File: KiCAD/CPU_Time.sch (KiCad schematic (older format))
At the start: 11 parts, among them P1 JST_connector, SW1 Reset, U1 NUCLEO64-F411RE, U2 DS3231, U3 MAS6180

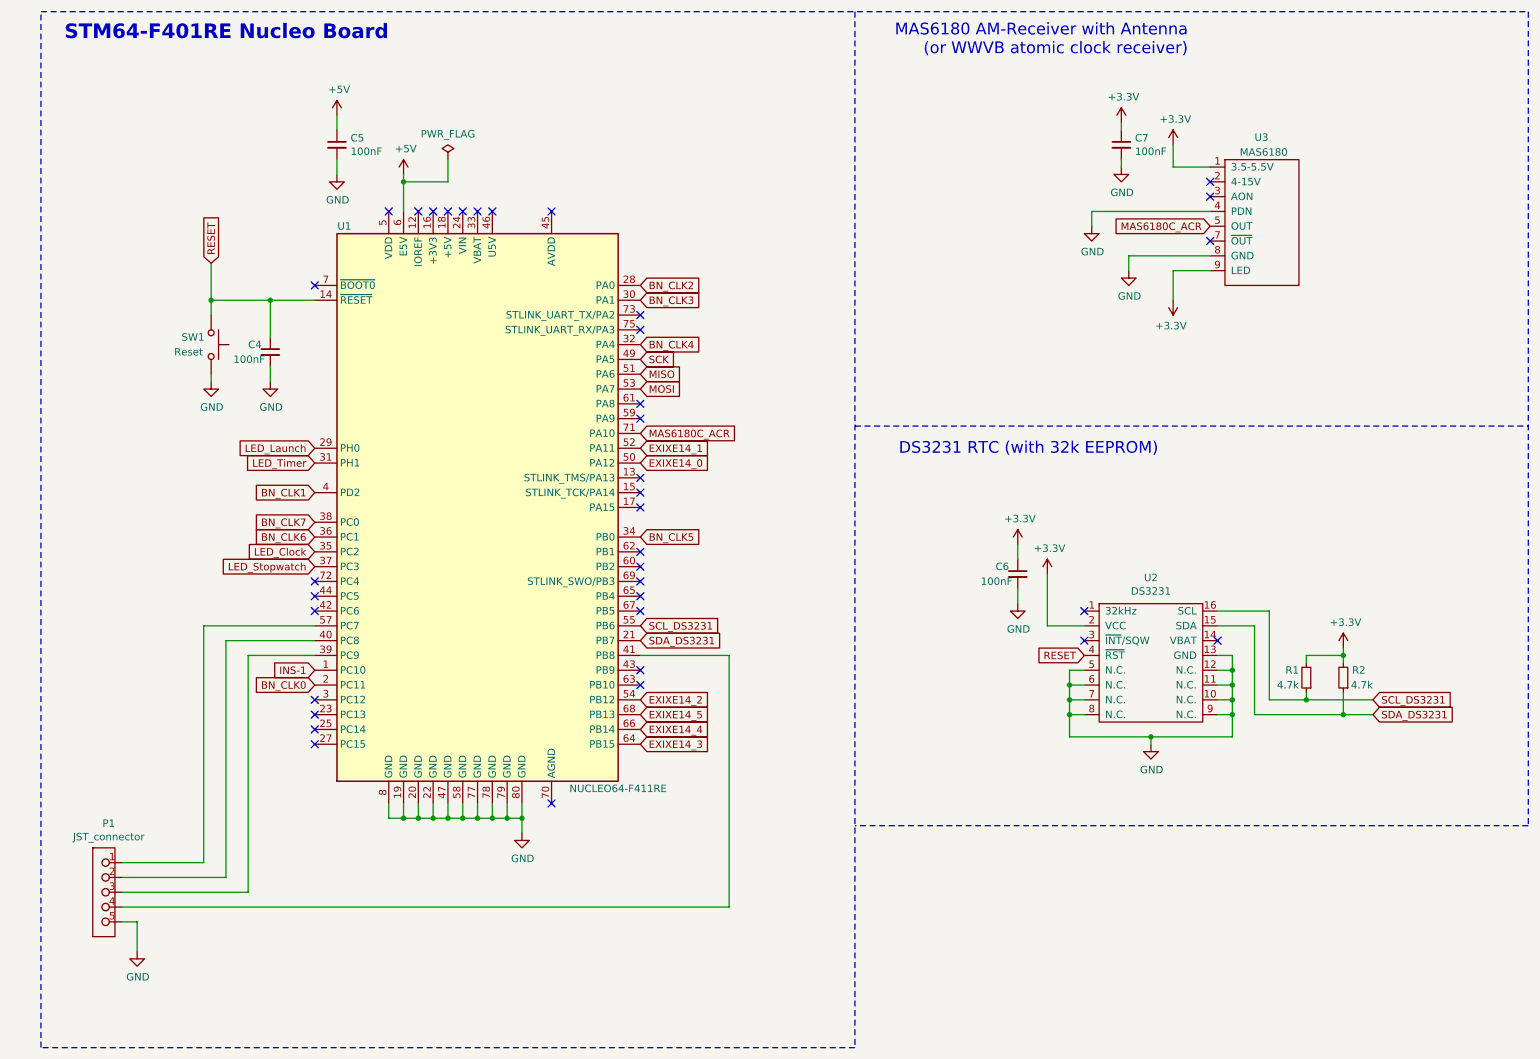
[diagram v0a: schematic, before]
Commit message: v01.2: Updated component numbers, title block, and added transistor library.
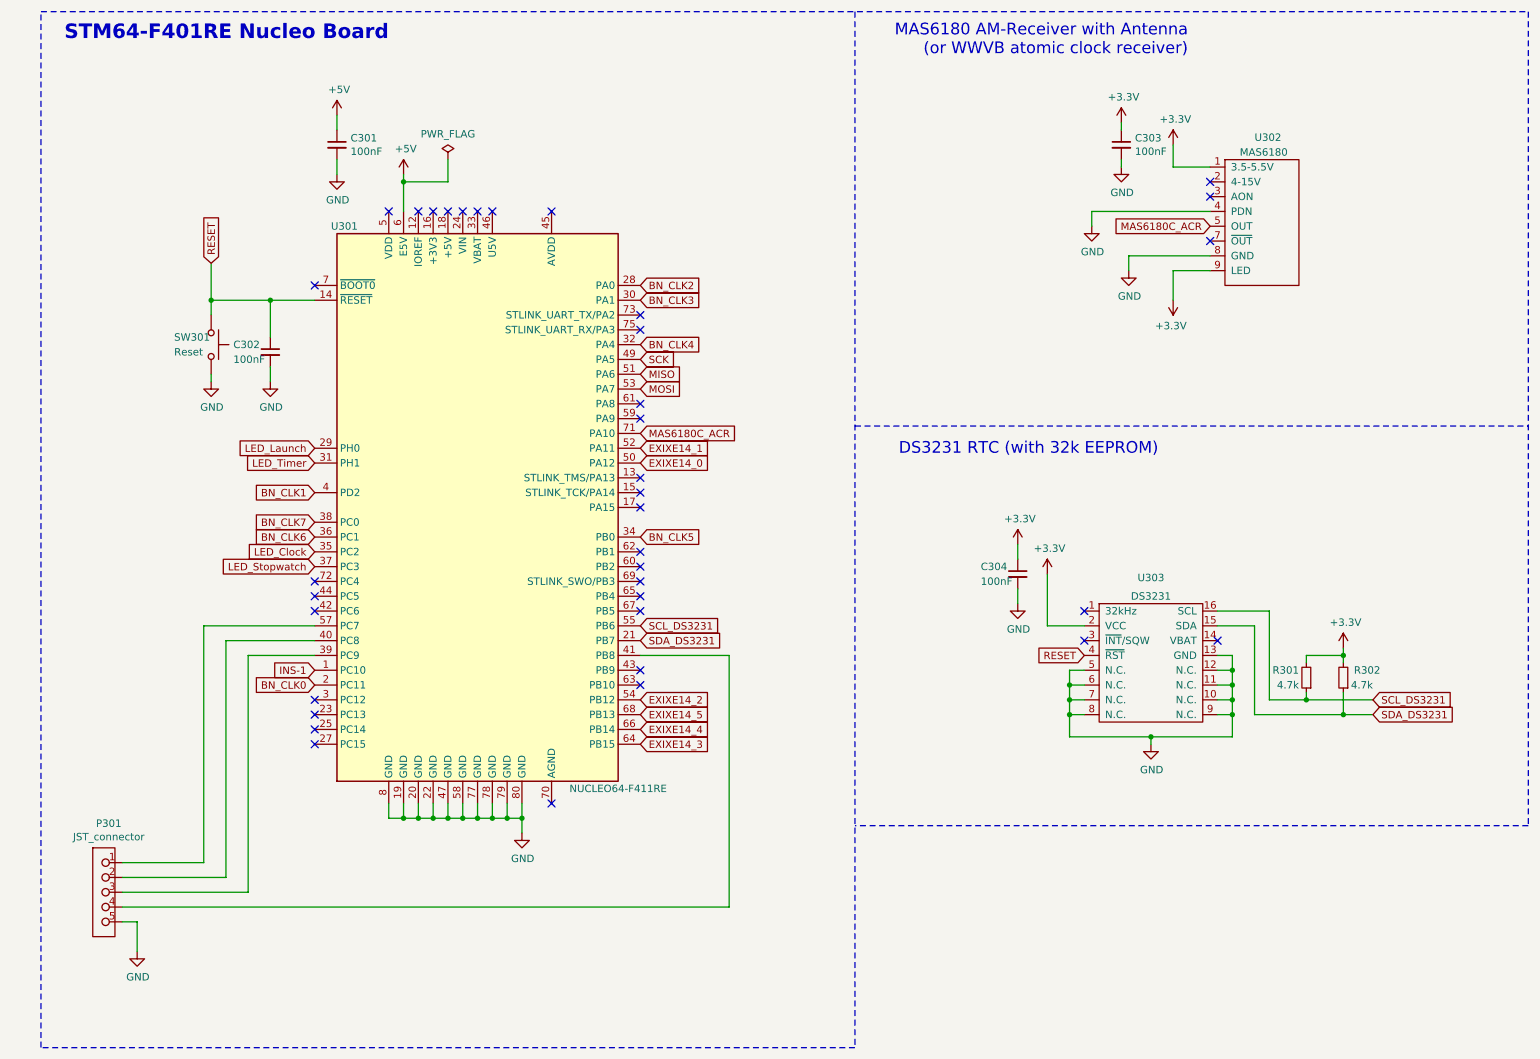
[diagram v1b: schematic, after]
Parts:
- renumbered C5 to C301, C4 to C302, C7 to C303, C6 to C304, P1 to P301, R1 to R301, R2 to R302, SW1 to SW301, U1 to U301, U3 to U302, U2 to U303
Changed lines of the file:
@@
 Sheet 3 5
 Title "Nixie Tube Clock Host Board"
-Date "2021-04-20"
-Rev "v01.1"
+Date "2021-04-26"
+Rev "v01.2"
 Comp "University of Alberta (AlbertaSat)"
-Comment1 "License: CC BY 4.0 (https://creativecommons.org/licenses/by/4.0/)"
-Comment2 "Steven Knudsen (ECE dept., Faculty of Engineering, University of Alberta)."
-Comment3 "This schematic was designed with the assistance of "
-Comment4 "Author: Pundeep Hundal                   Co-author: Sichun Xu"
+Comment1 ""
+Comment2 "License: CC BY 4.0 (https://creativecommons.org/licenses/by/4.0/)"
+Comment3 "Co-author: Sichun Xu"
+Comment4 "Author: Pundeep Hundal"
 $EndDescr
 $Comp
@@
 P 2550 2800
 AR Path="/6096D84C" Ref="C?"  Part="1"
-AR Path="/6091BF76/6096D84C" Ref="C4"  Part="1"
-F 0 "C4" H 2400 2850 50  0000 L CNN
+AR Path="/6091BF76/6096D84C" Ref="C302"  Part="1"
+F 0 "C302" H 2300 2850 50  0000 L CNN
 F 1 "100nF" H 2300 2750 50  0000 L CNN
 F 2 "" H 2550 2800 50  0001 C CNN
@@
 P 2150 2750
 AR Path="/6096D859" Ref="SW?"  Part="1"
-AR Path="/6091BF76/6096D859" Ref="SW1"  Part="1"
-F 0 "SW1" V 2100 2550 50  0000 L CNN
+AR Path="/6091BF76/6096D859" Ref="SW301"  Part="1"
+F 0 "SW301" V 2100 2500 50  0000 L CNN
 F 1 "Reset" V 2200 2500 50  0000 L CNN
 F 2 "" H 2150 2950 50  0001 C CNN
@@
 P 9250 1800
 AR Path="/6096D892" Ref="U?"  Part="1"
-AR Path="/6091BF76/6096D892" Ref="U3"  Part="1"
-F 0 "U3" H 9200 2250 50  0000 L CNN
+AR Path="/6091BF76/6096D892" Ref="U302"  Part="1"
+F 0 "U302" H 9200 2250 50  0000 L CNN
 F 1 "MAS6180" H 9100 2150 50  0000 L CNN
 F 2 "" H 9250 1800 50  0001 C CNN
@@
 P 7600 4300
 AR Path="/6096D898" Ref="C?"  Part="1"
-AR Path="/6091BF76/6096D898" Ref="C6"  Part="1"
-F 0 "C6" H 7450 4350 50  0000 L CNN
+AR Path="/6091BF76/6096D898" Ref="C304"  Part="1"
+F 0 "C304" H 7350 4350 50  0000 L CNN
 F 1 "100nF" H 7350 4250 50  0000 L CNN
 F 2 "" H 7600 4300 50  0001 C CNN
@@
 P 9800 5000
 AR Path="/6096D8BC" Ref="R?"  Part="1"
-AR Path="/6091BF76/6096D8BC" Ref="R2"  Part="1"
-F 0 "R2" H 9650 4950 50  0000 L CNN
+AR Path="/6091BF76/6096D8BC" Ref="R302"  Part="1"
+F 0 "R302" H 9550 4950 50  0000 L CNN
 F 1 "4.7k" H 9600 5050 50  0000 L CNN
 F 2 "" H 9800 5000 50  0001 C CNN
@@
 P 9550 5000
 AR Path="/6096D8C2" Ref="R?"  Part="1"
-AR Path="/6091BF76/6096D8C2" Ref="R1"  Part="1"
-F 0 "R1" H 9600 4950 50  0000 L CNN
+AR Path="/6091BF76/6096D8C2" Ref="R301"  Part="1"
+F 0 "R301" H 9600 4950 50  0000 L CNN
 F 1 "4.7k" H 9600 5050 50  0000 L CNN
 F 2 "" H 9550 5000 50  0001 C CNN
@@
 P 8500 4900
 AR Path="/6096D8EF" Ref="U?"  Part="1"
-AR Path="/6091BF76/6096D8EF" Ref="U2"  Part="1"
-F 0 "U2" H 8500 5475 50  0000 C CNN
-F 1 "DS3231" H 8500 5384 50  0000 C CNN
+AR Path="/6091BF76/6096D8EF" Ref="U303"  Part="1"
+F 0 "U303" H 8500 5475 50  0000 C CNN
+F 1 "DS3231" H 8500 5350 50  0000 C CNN
 F 2 "" H 8500 4900 50  0001 C CNN
 F 3 "" H 8500 4900 50  0001 C CNN
@@
 P 8300 1400
 AR Path="/6096D903" Ref="C?"  Part="1"
-AR Path="/6091BF76/6096D903" Ref="C7"  Part="1"
-F 0 "C7" H 8392 1446 50  0000 L CNN
+AR Path="/6091BF76/6096D903" Ref="C303"  Part="1"
+F 0 "C303" H 8392 1446 50  0000 L CNN
 F 1 "100nF" H 8392 1355 50  0000 L CNN
 F 2 "" H 8300 1400 50  0001 C CNN
@@
 P 1550 6450
 AR Path="/6096D911" Ref="P?"  Part="1"
-AR Path="/6091BF76/6096D911" Ref="P1"  Part="1"
-F 0 "P1" H 1458 6915 50  0000 C CNN
+AR Path="/6091BF76/6096D911" Ref="P301"  Part="1"
+F 0 "P301" H 1458 6915 50  0000 C CNN
 F 1 "JST_connector" H 1458 6824 50  0000 C CNN
 F 2 "" H 1550 6450 50  0001 C CNN
@@
 P 3000 1400
 AR Path="/6089E69D" Ref="C?"  Part="1"
-AR Path="/6091BF76/6089E69D" Ref="C5"  Part="1"
-F 0 "C5" H 3092 1446 50  0000 L CNN
+AR Path="/6091BF76/6089E69D" Ref="C301"  Part="1"
+F 0 "C301" H 3092 1446 50  0000 L CNN
 F 1 "100nF" H 3092 1355 50  0000 L CNN
 F 2 "" H 3000 1400 50  0001 C CNN
@@
 $EndComp
 $Comp
-L MCU_Module:NUCLEO64-F411RE U1
+L MCU_Module:NUCLEO64-F411RE U301
 U 1 1 608AA55B
 P 3950 3850
-F 0 "U1" H 3050 5750 50  0000 C CNN
+F 0 "U301" H 3050 5750 50  0000 C CNN
 F 1 "NUCLEO64-F411RE" H 4900 1950 50  0000 C CNN
 F 2 "Module:ST_Morpho_Connector_144_STLink" H 4500 1950 50  0001 L CNN
